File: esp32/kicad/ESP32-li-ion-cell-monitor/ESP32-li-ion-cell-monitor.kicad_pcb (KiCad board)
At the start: 2 copper layers, 78 x 26 mm, 105 parts, among them J1 Conn_01x01_Female, J2 Conn_01x01_Female, J3 Conn_01x05_Male, Q1 Q_NMOS_GSD, Q2 Q_NMOS_GSD, Q3 Q_NMOS_GSD, Q4 Q_NMOS_GSD, U1 NCP186B, U2 ES-WROOM-32, U3 INA219_SOT23-8, U4 Si7060-00, U5 Si7060-01

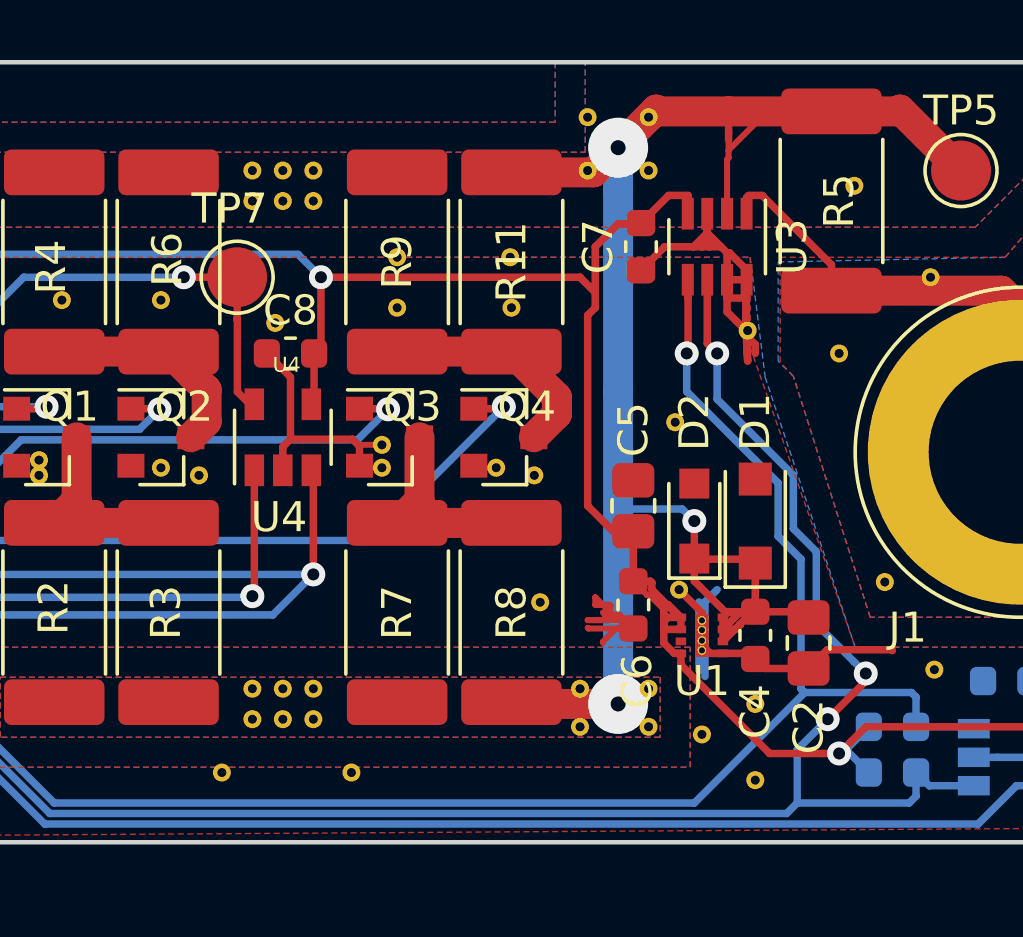
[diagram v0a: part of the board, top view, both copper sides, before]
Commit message: XDFN8 Footprint flaw
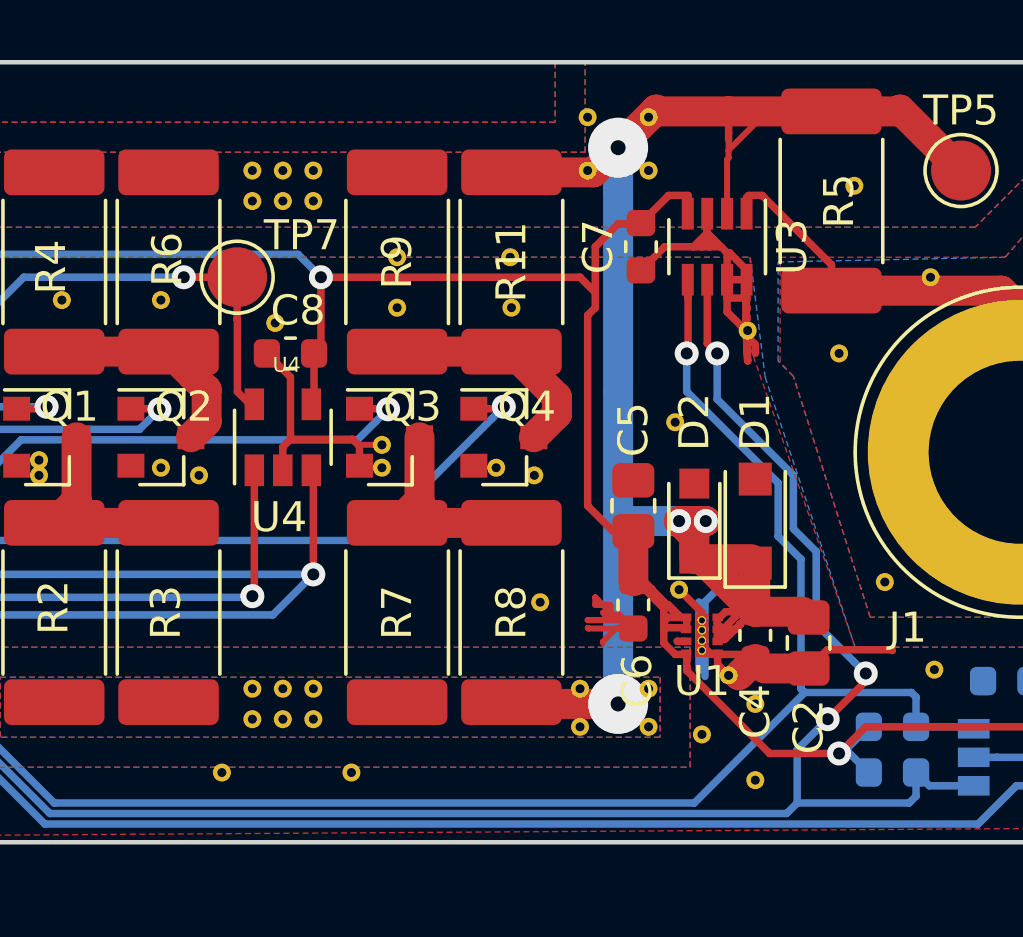
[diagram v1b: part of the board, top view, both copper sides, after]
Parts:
- added REF**: Via-0.6mm, module:Via-0.6mm, F.Cu at (216.3, 71.4)
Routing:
- net VCC: track 68.6 -> 73.0 mm, vias 3 -> 4
- net GND: track 51.4 -> 53.4 mm
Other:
- board text added: "ESP32 Li-Ion Cell Monitor Rev. 1.1 1831"
- board text removed: "ESP32 Li-Ion Cell Monitor Rev. 1.0 1826"
